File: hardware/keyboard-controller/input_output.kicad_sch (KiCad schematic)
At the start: 20 parts

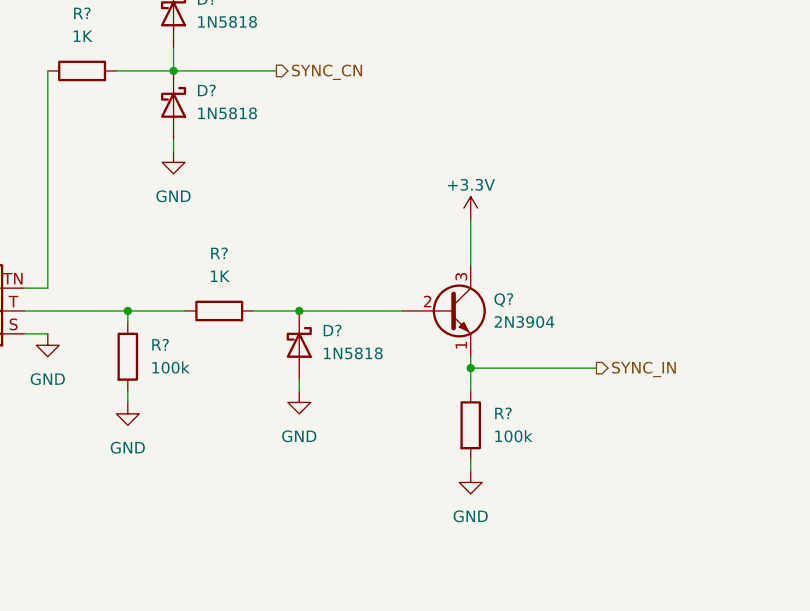
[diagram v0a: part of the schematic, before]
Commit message: Added filter caps on pots and rotary switches
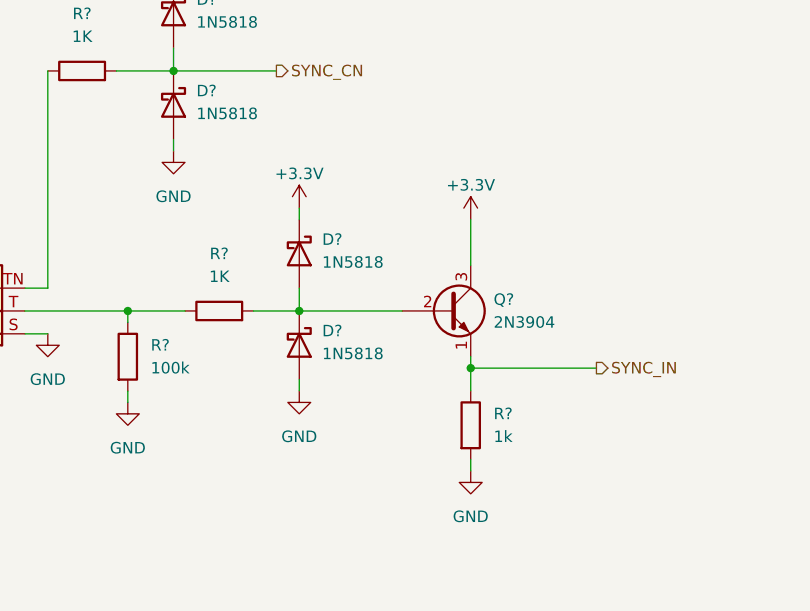
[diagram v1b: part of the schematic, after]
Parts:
- added D?: 1N5818, Diode_THT:D_DO-41_SOD81_P10.16mm_Horizontal, symbol Diode:1N5818
- R?: value 100k -> 1k
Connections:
- net +3V3: now also D?.1 (K)
- net at D?.1 (K), Q?.2 (B), R?.2: now also D?.2 (A)
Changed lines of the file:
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@@
+    (stroke (width 0) (type default) (color 0 0 0 0))
+  )
+  (wire (pts (xy 93.98 87.63) (xy 93.98 90.17))
     (stroke (width 0) (type default) (color 0 0 0 0))
   )
@@
   )
   (wire (pts (xy 209.55 68.58) (xy 210.82 68.58))
+    (stroke (width 0) (type default) (color 0 0 0 0))
+  )
+  (wire (pts (xy 93.98 78.74) (xy 93.98 80.01))
     (stroke (width 0) (type default) (color 0 0 0 0))
   )
@@
       (effects (font (size 1.27 1.27)) (justify left))
     )
-    (property "Value" "100k" (id 1) (at 115.57 104.1399 0)
+    (property "Value" "1k" (id 1) (at 115.57 104.1399 0)
       (effects (font (size 1.27 1.27)) (justify left))
     )
@@
     (pin "1")
   )
+  (symbol (lib_id "Diode:1N5818") (at 93.98 83.82 270) (unit 1)
+    (in_bom yes) (on_board yes) (fields_autoplaced)
+    (property "Reference" "D?" (id 0) (at 96.52 82.2324 90)
+      (effects (font (size 1.27 1.27)) (justify left))
+    )
+    (property "Value" "1N5818" (id 1) (at 96.52 84.7724 90)
+      (effects (font (size 1.27 1.27)) (justify left))
+    )
+    (property "Footprint" "Diode_THT:D_DO-41_SOD81_P10.16mm_Horizontal" (id 2) (at 89.535 83.82 0)
+      (effects (font (size 1.27 1.27)) hide)
+    )
+    (property "Datasheet" "http://www.vishay.com/docs/88525/1n5817.pdf" (id 3) (at 93.98 83.82 0)
+      (effects (font (size 1.27 1.27)) hide)
+    )
+    (pin "1")
+    (pin "2")
+  )
   (symbol (lib_id "Device:R") (at 193.04 82.55 0) (unit 1)
     (in_bom yes) (on_board yes) (fields_autoplaced)
@@
     (pin "2")
   )
+  (symbol (lib_id "power:+3.3V") (at 93.98 78.74 0) (unit 1)
+    (in_bom yes) (on_board yes)
+    (property "Reference" "#PWR?" (id 0) (at 93.98 82.55 0)
+      (effects (font (size 1.27 1.27)) hide)
+    )
+    (property "Value" "+3.3V" (id 1) (at 93.98 74.93 0))
+    (property "Footprint" "" (id 2) (at 93.98 78.74 0)
+      (effects (font (size 1.27 1.27)) hide)
+    )
+    (property "Datasheet" "" (id 3) (at 93.98 78.74 0)
+      (effects (font (size 1.27 1.27)) hide)
+    )
+    (pin "1")
+  )
   (symbol (lib_id "power:GND") (at 226.06 73.66 0) (unit 1)

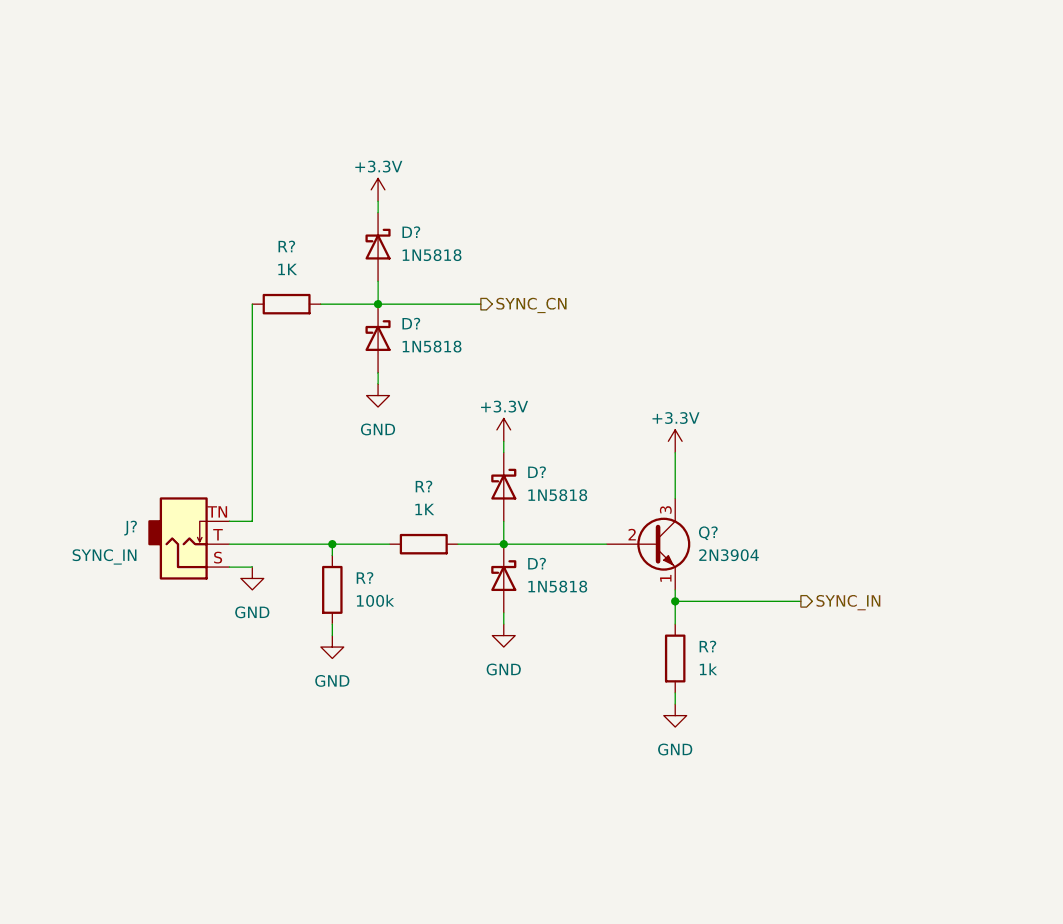
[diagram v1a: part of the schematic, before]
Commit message: Added analog switch for analog input
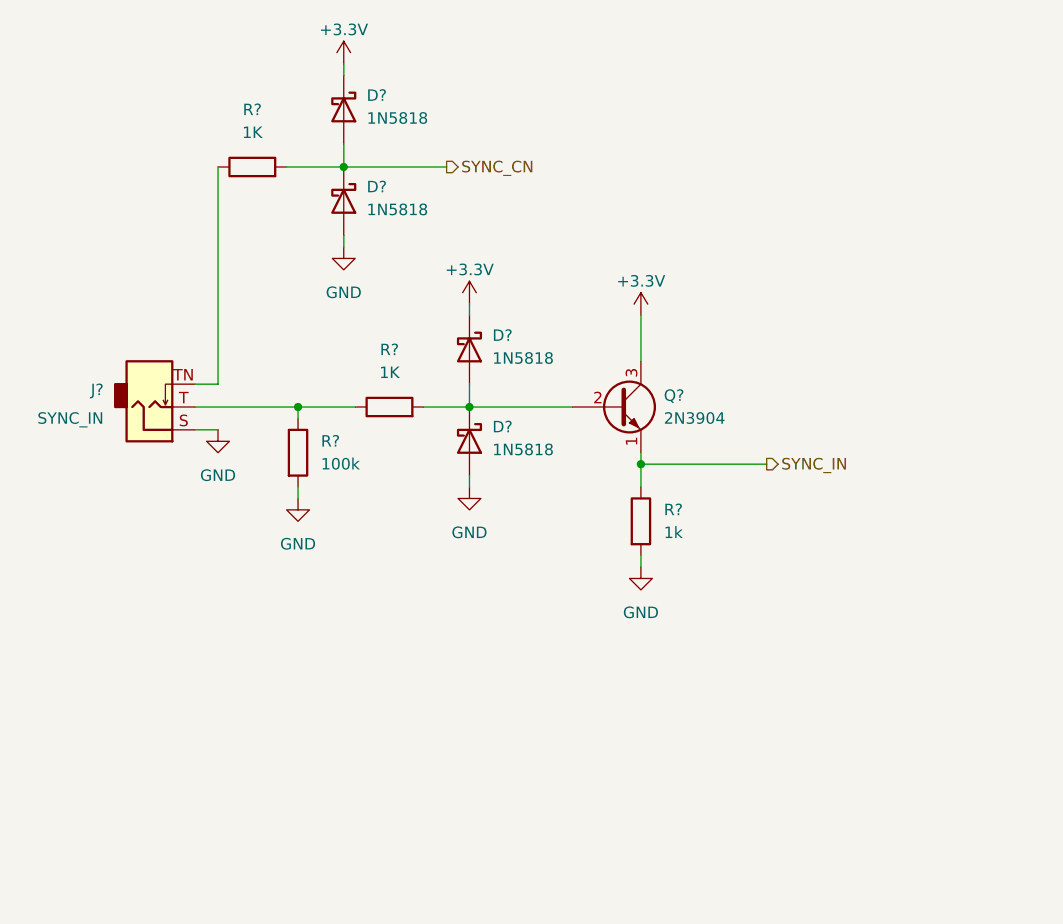
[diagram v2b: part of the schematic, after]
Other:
- title: (none) -> Input/Output Jacks
- moved on the sheet: D?, J?, Q?, R?

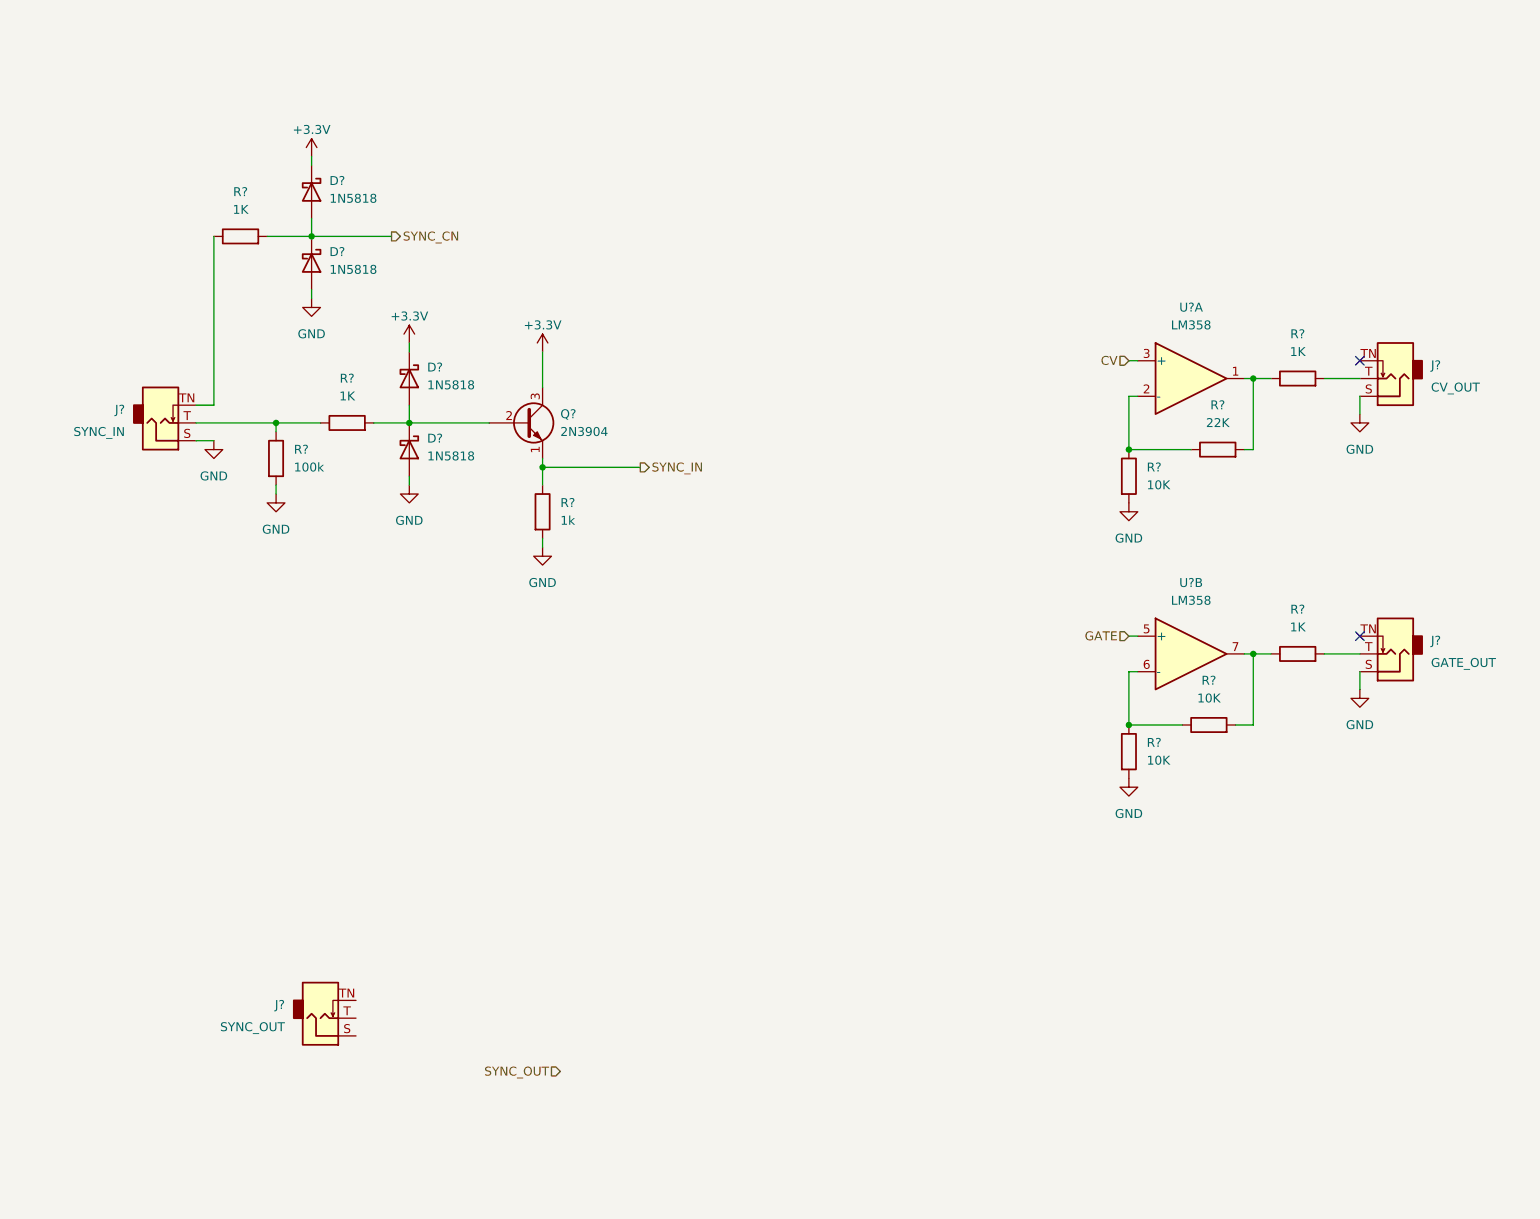
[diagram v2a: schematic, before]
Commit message: Added footprint for rotary switches
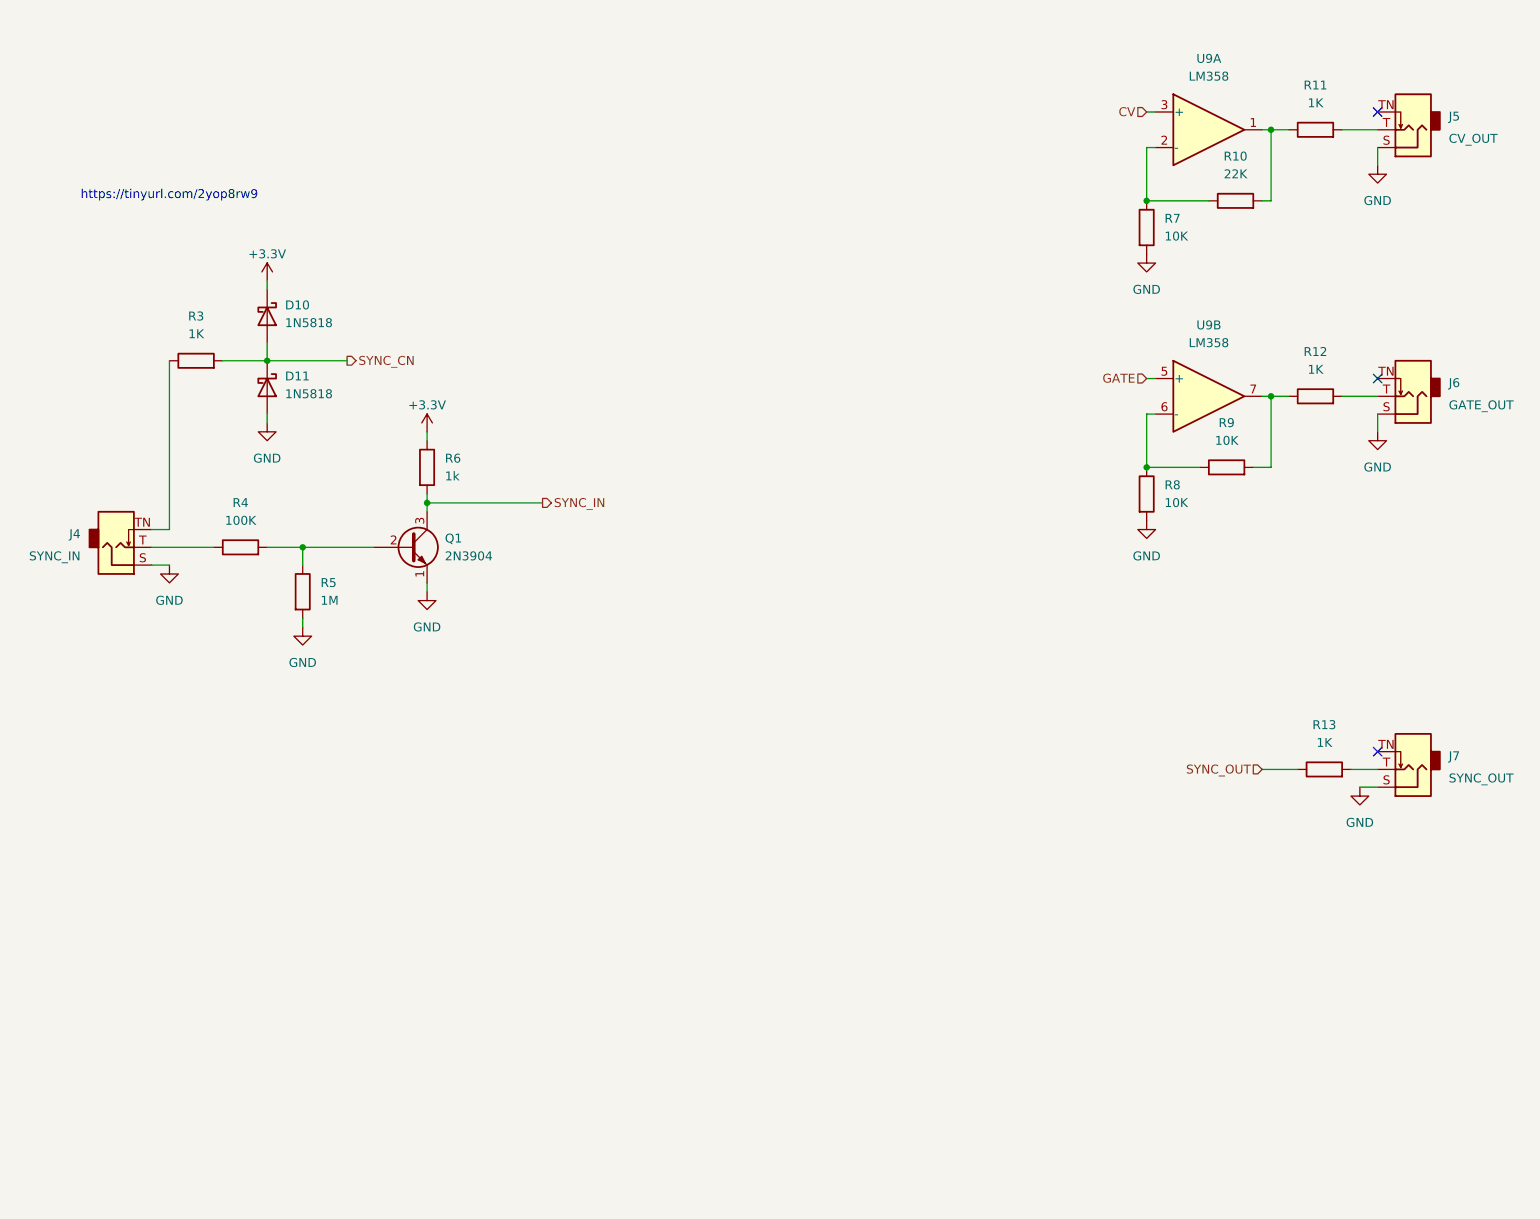
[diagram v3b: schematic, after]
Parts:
- removed D? (x2): 1N5818, Diode_THT:D_DO-41_SOD81_P10.16mm_Horizontal, symbol Diode:1N5818
- removed R?: 1k, symbol Device:R
- added R13: 1K, symbol Device:R
- added R6: 1k, symbol Device:R
- R4: renamed from R?; value 1K -> 100K
- R5: renamed from R?; value 100k -> 1M
- gave numbers to parts that had none: 15
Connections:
- net +3V3: now also R6.1; no longer Q1.3 (C)
- net GND: now also J7.S, Q1.1 (E)
- net SYNC_IN: now also Q1.3 (C), R6.2; no longer Q1.1 (E)
- net SYNC_OUT: now also R13.1
- net at J4.T, R4.1: no longer R5.1
- net at Q1.2 (B), R4.2: now also R5.1
- net at J7.T: now also R13.2
- no-connect marks 2 -> 3
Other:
- note added: "https://tinyurl.com/2yop8rw9"
- moved on the sheet: D10, D11, J4, J5, J6, J7, Q1, R10, R11, R12, R3, R4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

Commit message: Updated hardware_config and fixed sync_cn
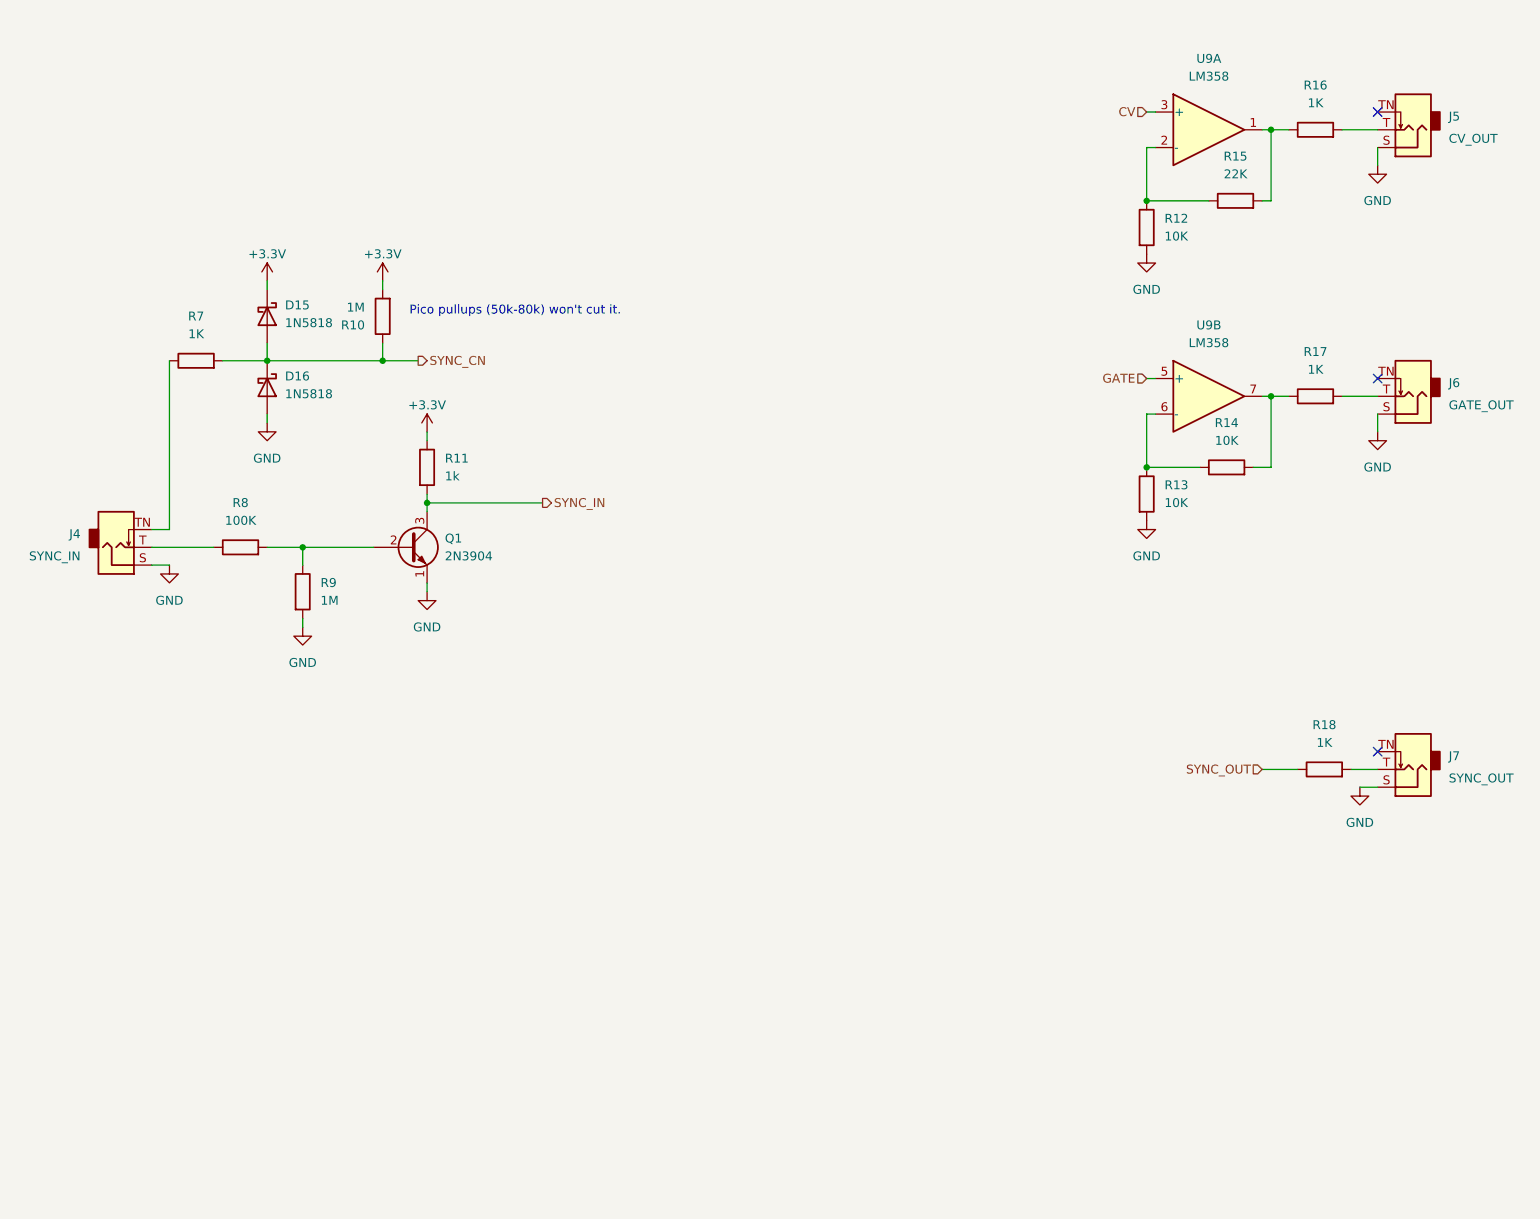
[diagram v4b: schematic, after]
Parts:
- added R10: 1M, symbol Device:R
- D15: renamed from D10; Supplier (none) -> Tayda
- D16: renamed from D11; Supplier (none) -> Tayda
- Q1, U9: Supplier (none) -> Tayda
- R11: renamed from R6; Supplier (none) -> Tayda
- R18: renamed from R13; Supplier (none) -> Tayda
- R7: renamed from R3; Supplier (none) -> Tayda
- R8: renamed from R4; Supplier (none) -> Tayda
- R9: renamed from R5; Supplier (none) -> Tayda
- renumbered R7 to R12, R8 to R13, R9 to R14, R10 to R15, R11 to R16, R12 to R17
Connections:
- net +3V3: now also R10.2
- net SYNC_CN: now also R10.1
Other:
- note added: "Pico pullups (50k-80k) won't cut it."
- note removed: "https://tinyurl.com/2yop8rw9"
